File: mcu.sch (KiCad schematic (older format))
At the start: 1 part

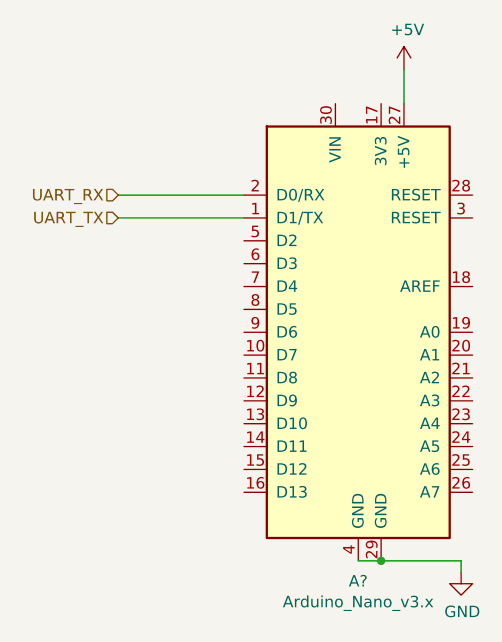
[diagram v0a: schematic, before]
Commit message: Added switching, still need arduino verification, need buffer, consisder PSU polarity switch
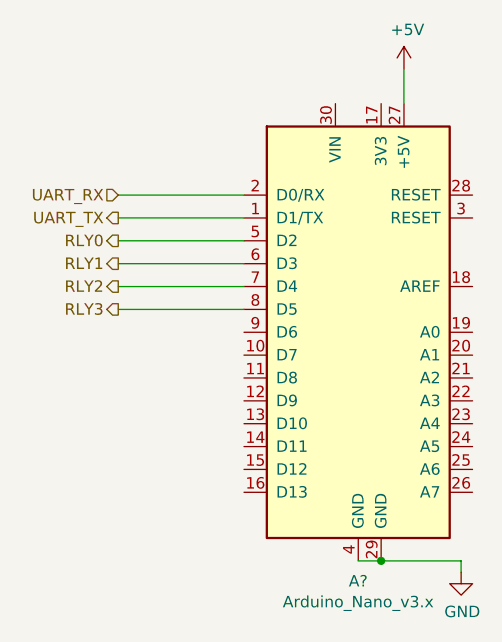
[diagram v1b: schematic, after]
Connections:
- net RLY0: now reaches A?.5 (D2)
- net RLY1: now reaches A?.6 (D3)
- net RLY2: now reaches A?.7 (D4)
- net RLY3: now reaches A?.8 (D5)
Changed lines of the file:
@@
 Text HLabel 4350 2700 0    50   Input ~ 0
 UART_RX
-Text HLabel 4350 2800 0    50   Input ~ 0
+Text HLabel 4350 2800 0    50   Output ~ 0
 UART_TX
 Wire Wire Line
@@
 Wire Wire Line
 	4900 2800 4350 2800
+Text HLabel 4350 2900 0    50   Output ~ 0
+RLY0
+Text HLabel 4350 3000 0    50   Output ~ 0
+RLY1
+Text HLabel 4350 3100 0    50   Output ~ 0
+RLY2
+Text HLabel 4350 3200 0    50   Output ~ 0
+RLY3
+Wire Wire Line
+	4900 2900 4350 2900
+Wire Wire Line
+	4900 3000 4350 3000
+Wire Wire Line
+	4900 3100 4350 3100
+Wire Wire Line
+	4900 3200 4350 3200
 $EndSCHEMATC

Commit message: Schem entry done, need to do footprints and PCB
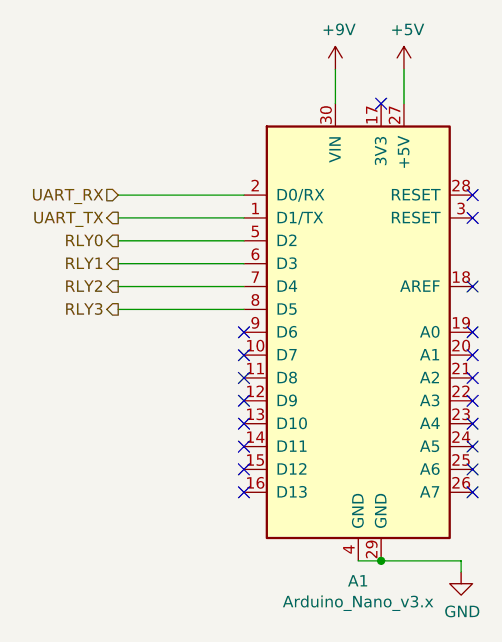
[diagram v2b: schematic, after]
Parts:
- gave numbers to parts that had none: 1
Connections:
- net +9V: now reaches A1.30 (VIN)
- no-connect marks 0 -> 20
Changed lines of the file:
@@
 EESchema Schematic File Version 4
 LIBS:midi_switcher-cache
-EELAYER 29 0
+EELAYER 30 0
 EELAYER END
 $Descr A4 11693 8268
@@
 $EndDescr
 $Comp
-L MCU_Module:Arduino_Nano_v3.x A?
+L MCU_Module:Arduino_Nano_v3.x A1
 U 1 1 5D74B459
 P 5400 3300
-F 0 "A?" H 5400 2211 50  0000 C CNN
+F 0 "A1" H 5400 2211 50  0000 C CNN
 F 1 "Arduino_Nano_v3.x" H 5400 2120 50  0000 C CNN
 F 2 "Module:Arduino_Nano" H 5550 2350 50  0001 L CNN
@@
 	5400 4300 5500 4300
 $Comp
-L power:GND #PWR?
+L power:GND #PWR0107
 U 1 1 5D74C7F9
 P 5850 4350
-F 0 "#PWR?" H 5850 4100 50  0001 C CNN
+F 0 "#PWR0107" H 5850 4100 50  0001 C CNN
 F 1 "GND" H 5855 4177 50  0000 C CNN
 F 2 "" H 5850 4350 50  0001 C CNN
@@
 	5600 2300 5600 2150
 $Comp
-L power:+5V #PWR?
+L power:+5V #PWR0108
 U 1 1 5D74DD5E
 P 5600 2150
-F 0 "#PWR?" H 5600 2000 50  0001 C CNN
+F 0 "#PWR0108" H 5600 2000 50  0001 C CNN
 F 1 "+5V" H 5615 2323 50  0000 C CNN
 F 2 "" H 5600 2150 50  0001 C CNN
@@
 Wire Wire Line
 	4900 3200 4350 3200
+$Comp
+L power:+9V #PWR0109
+U 1 1 5DC8F515
+P 5300 2150
+F 0 "#PWR0109" H 5300 2000 50  0001 C CNN
+F 1 "+9V" H 5315 2323 50  0000 C CNN
+F 2 "" H 5300 2150 50  0001 C CNN
+F 3 "" H 5300 2150 50  0001 C CNN
+	1    5300 2150
+	1    0    0    -1
+$EndComp
+Wire Wire Line
+	5300 2150 5300 2300
+NoConn ~ 4900 3300
+NoConn ~ 4900 3400
+NoConn ~ 4900 3500
+NoConn ~ 4900 3600
+NoConn ~ 4900 3700
+NoConn ~ 4900 3800
+NoConn ~ 4900 3900
+NoConn ~ 4900 4000
+NoConn ~ 5900 2700
+NoConn ~ 5900 2800
+NoConn ~ 5900 3100
+NoConn ~ 5900 3300
+NoConn ~ 5900 3400
+NoConn ~ 5900 3500
+NoConn ~ 5900 3600
+NoConn ~ 5900 3700
+NoConn ~ 5900 3800
+NoConn ~ 5900 3900
+NoConn ~ 5900 4000
+NoConn ~ 5500 2300
 $EndSCHEMATC
